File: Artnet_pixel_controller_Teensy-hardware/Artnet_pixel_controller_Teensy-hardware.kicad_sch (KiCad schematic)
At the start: 37 parts, among them J1 Barrel_Jack_Switch, J10 Conn_01x02_Pin, J2 HR871181A, J3 Conn_01x02_Pin, J4 Conn_01x02_Pin, J5 Conn_01x02_Pin, J6 Conn_01x02_Pin, J7 Conn_01x02_Pin, J8 Conn_01x02_Pin, J9 Conn_01x02_Pin, Q1 AO3401A, SW1 SW_DIP_x08, U1 R-785.0-1.0, U3 74HC245

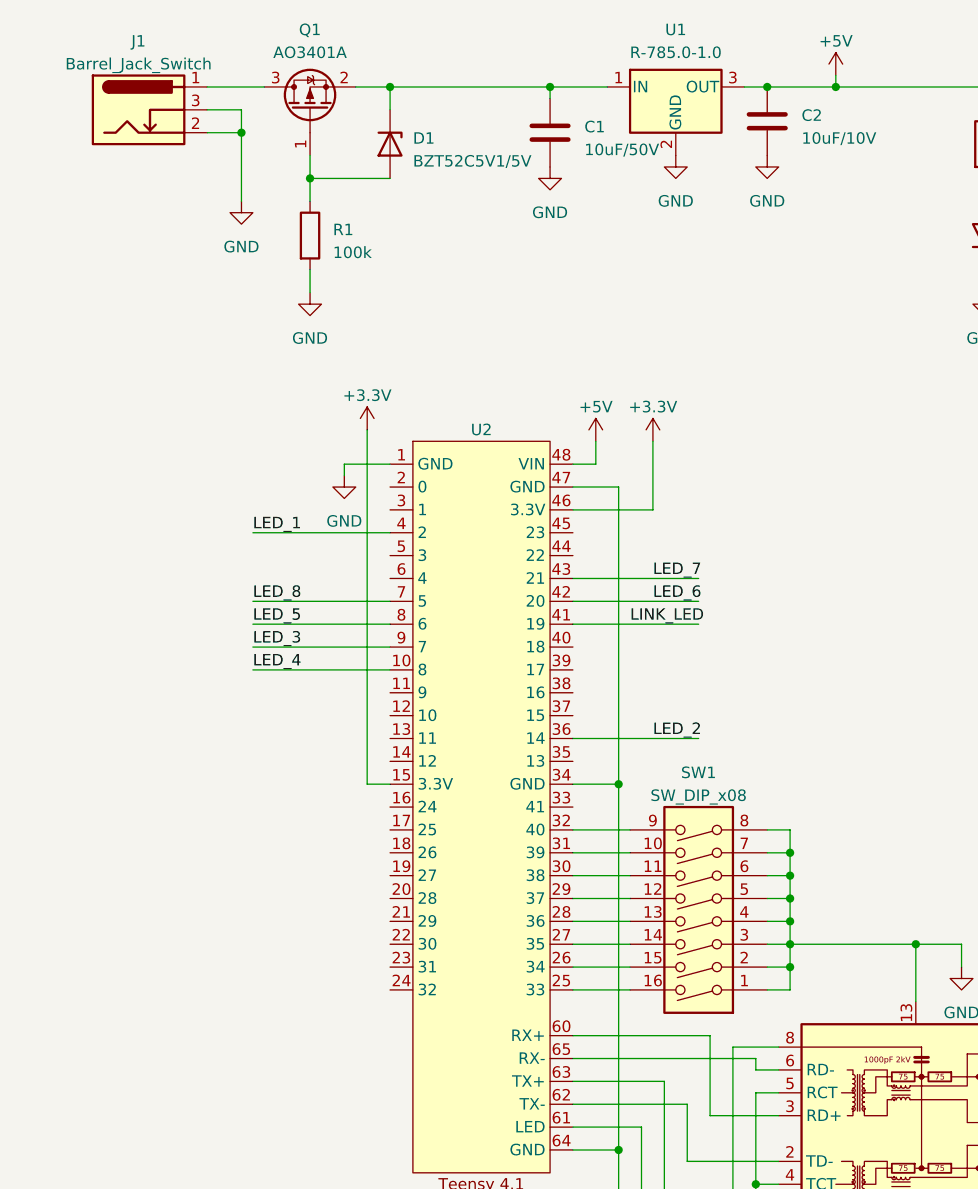
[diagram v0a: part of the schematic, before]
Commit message: WS2812Serial用のピン配置に変更
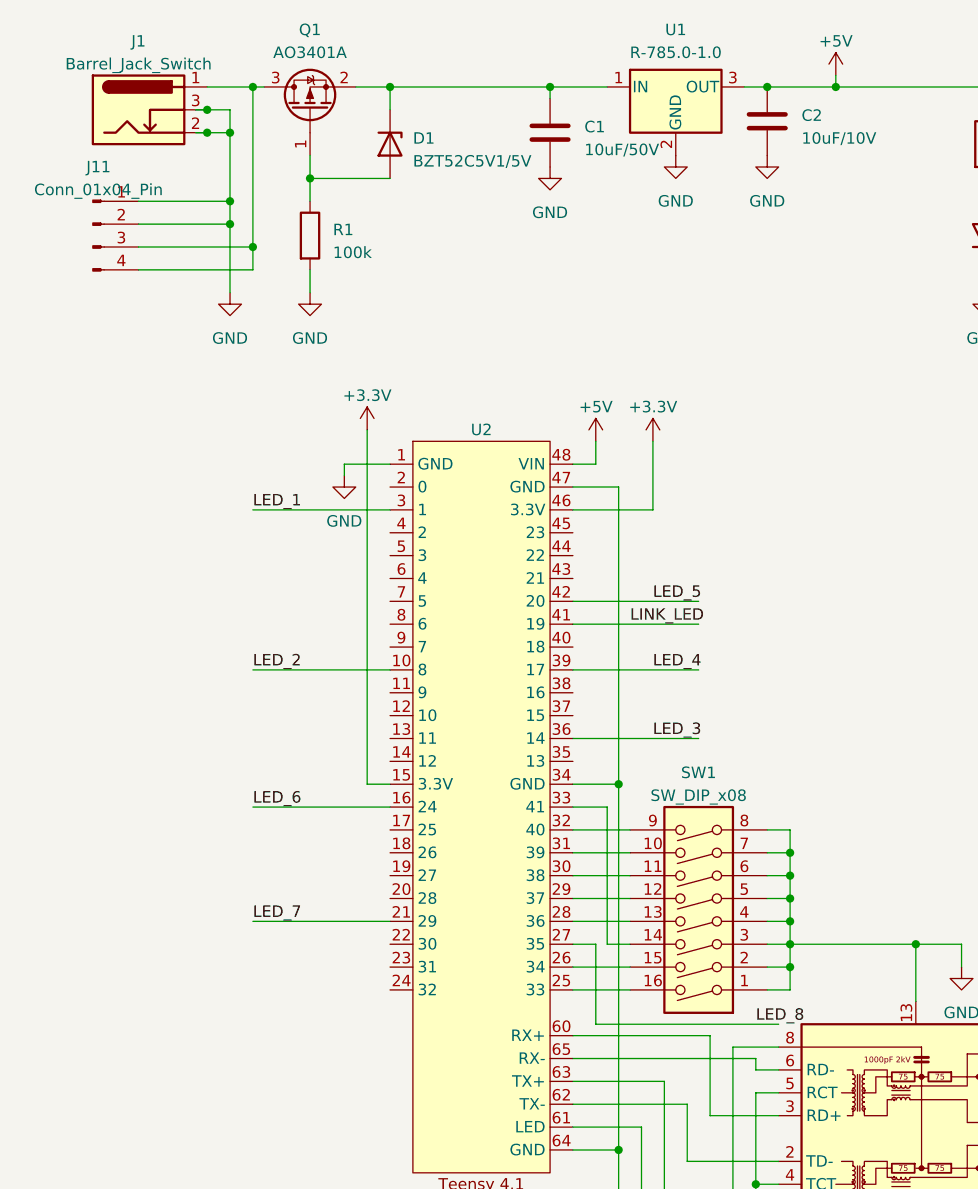
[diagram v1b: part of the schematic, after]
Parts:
- added J11: Conn_01x04_Pin, Connector_Phoenix_MC:PhoenixContact_MC_1,5_4-G-3.81_1x04_P3.81mm_Horizontal, symbol Connector:Conn_01x04_Pin
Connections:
- net GND: now also J11.1 (Pin_1), J11.2 (Pin_2)
- net LED_1: now also U2.3 (1); no longer U2.4 (2)
- net LED_2: now also U2.10 (8); no longer U2.36 (14)
- net LED_3: now also U2.36 (14); no longer U2.9 (7)
- net LED_4: now also U2.39 (17); no longer U2.10 (8)
- net LED_5: now also U2.42 (20); no longer U2.8 (6)
- net LED_6: now also U2.16 (24); no longer U2.42 (20)
- net LED_7: now also U2.21 (29); no longer U2.43 (21)
- net LED_8: now also U2.27 (35); no longer U2.7 (5)
- net at J1.1, Q1.3 (D): now also J11.3 (Pin_3), J11.4 (Pin_4)
- net at SW1.14: now also U2.33 (41); no longer U2.27 (35)
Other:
- company: (none) -> Ponoor Experiments inc.
- title: (none) -> Artnet pixel led controller with Teensy4.1

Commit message: プロト基板入稿データ
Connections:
- net +3.3V: no longer names the net of U2.15 (3.3V)
- net +3.3V: no longer U2.46 (3.3V)
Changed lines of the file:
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@@
-    (stroke (width 0) (type default))
-  )
-  (wire (pts (xy 60.96 106.68) (xy 58.42 106.68))
     (stroke (width 0) (type default))
   )
@@
     (stroke (width 0) (type default))
   )
-  (wire (pts (xy 81.28 76.2) (xy 90.17 76.2))
-    (stroke (width 0) (type default))
-  )
   (wire (pts (xy 52.07 49.53) (xy 52.07 52.07))
     (stroke (width 0) (type default))
@@
     (stroke (width 0) (type default))
   )
-  (wire (pts (xy 90.17 68.58) (xy 90.17 76.2))
-    (stroke (width 0) (type default))
-  )
   (wire (pts (xy 227.33 71.12) (xy 233.68 71.12))
     (stroke (width 0) (type default))
@@
   )
   (wire (pts (xy 81.28 106.68) (xy 86.36 106.68))
-    (stroke (width 0) (type default))
-  )
-  (wire (pts (xy 58.42 106.68) (xy 58.42 67.31))
     (stroke (width 0) (type default))
   )
@@
         (path "/92745dad-aaf3-4218-9787-63c390caac23"
           (reference "H5") (unit 1)
-        )
-      )
-    )
-  )
-  (symbol (lib_id "power:+3.3V") (at 90.17 68.58 0) (unit 1)
-    (in_bom yes) (on_board yes) (dnp no) (fields_autoplaced)
-    (property "Reference" "#PWR09" (at 90.17 72.39 0)
-      (effects (font (size 1.27 1.27)) hide)
-    )
-    (property "Value" "+3.3V" (at 90.17 64.77 0)
-      (effects (font (size 1.27 1.27)))
-    )
-    (property "Footprint" "" (at 90.17 68.58 0)
-      (effects (font (size 1.27 1.27)) hide)
-    )
-    (property "Datasheet" "" (at 90.17 68.58 0)
-      (effects (font (size 1.27 1.27)) hide)
-    )
-    (pin "1")
-    (instances
-      (project "Artnet_pixel_controller_Teensy-hardware"
-        (path "/92745dad-aaf3-4218-9787-63c390caac23"
-          (reference "#PWR09") (unit 1)
         )
       )
@@
         )
       )
-    )
-  )
-  (symbol (lib_id "power:+3.3V") (at 58.42 67.31 0) (unit 1)
-    (in_bom yes) (on_board yes) (dnp no) (fields_autoplaced)
-    (property "Reference" "#PWR011" (at 58.42 71.12 0)
-      (effects (font (size 1.27 1.27)) hide)
-    )
-    (property "Value" "+3.3V" (at 58.42 63.5 0)
-      (effects (font (size 1.27 1.27)))
-    )
-    (property "Footprint" "" (at 58.42 67.31 0)
-      (effects (font (size 1.27 1.27)) hide)
-    )
-    (property "Datasheet" "" (at 58.42 67.31 0)
-      (effects (font (size 1.27 1.27)) hide)
-    )
-    (pin "1")
-    (instances
-      (project "Artnet_pixel_controller_Teensy-hardware"
-        (path "/92745dad-aaf3-4218-9787-63c390caac23"
-          (reference "#PWR011") (unit 1)
-        )
-      )

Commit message: gerber data v1.0.0
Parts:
- R1: value 100k -> 10k
- R11: value 1k -> 10k
- R2: value 150 -> 220
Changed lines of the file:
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@@
       (effects (font (size 1.27 1.27)) (justify left))
     )
-    (property "Value" "1k" (at 129.54 37.465 0)
+    (property "Value" "10k" (at 129.54 37.465 0)
       (effects (font (size 1.27 1.27)) (justify left))
     )
@@
       (effects (font (size 1.27 1.27)))
     )
-    (property "Value" "150" (at 129.54 165.1 90)
+    (property "Value" "220" (at 129.54 165.1 90)
       (effects (font (size 1.27 1.27)))
     )
@@
       (effects (font (size 1.27 1.27)) (justify left))
     )
-    (property "Value" "100k" (at 54.61 47.625 0)
-      (effects (font (size 1.27 1.27)) (justify left))
-    )
+    (property "Value" "10k" (at 54.61 47.625 0)
+      (effects (font (size 1.27 1.27)) (justify left))
+    )

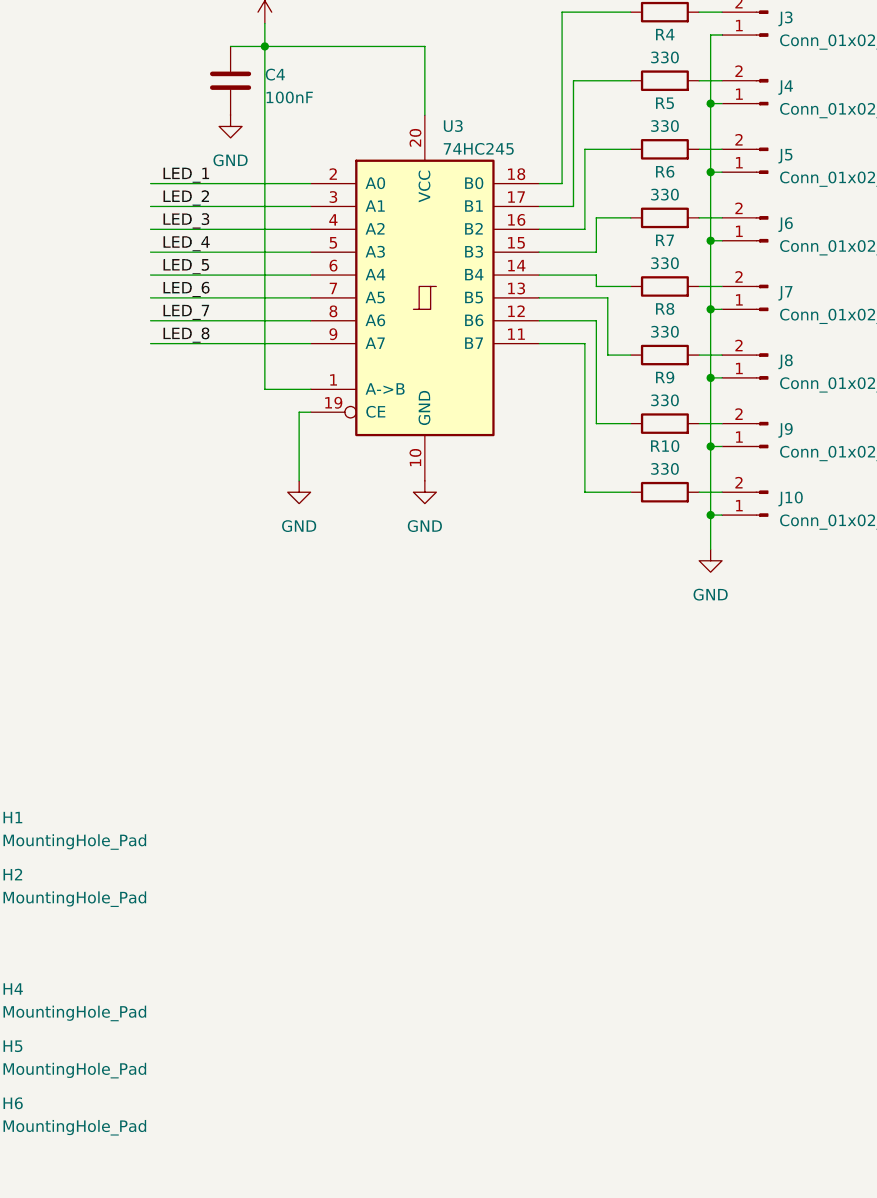
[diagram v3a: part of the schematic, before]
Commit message: LED出力の番号を入れ替え
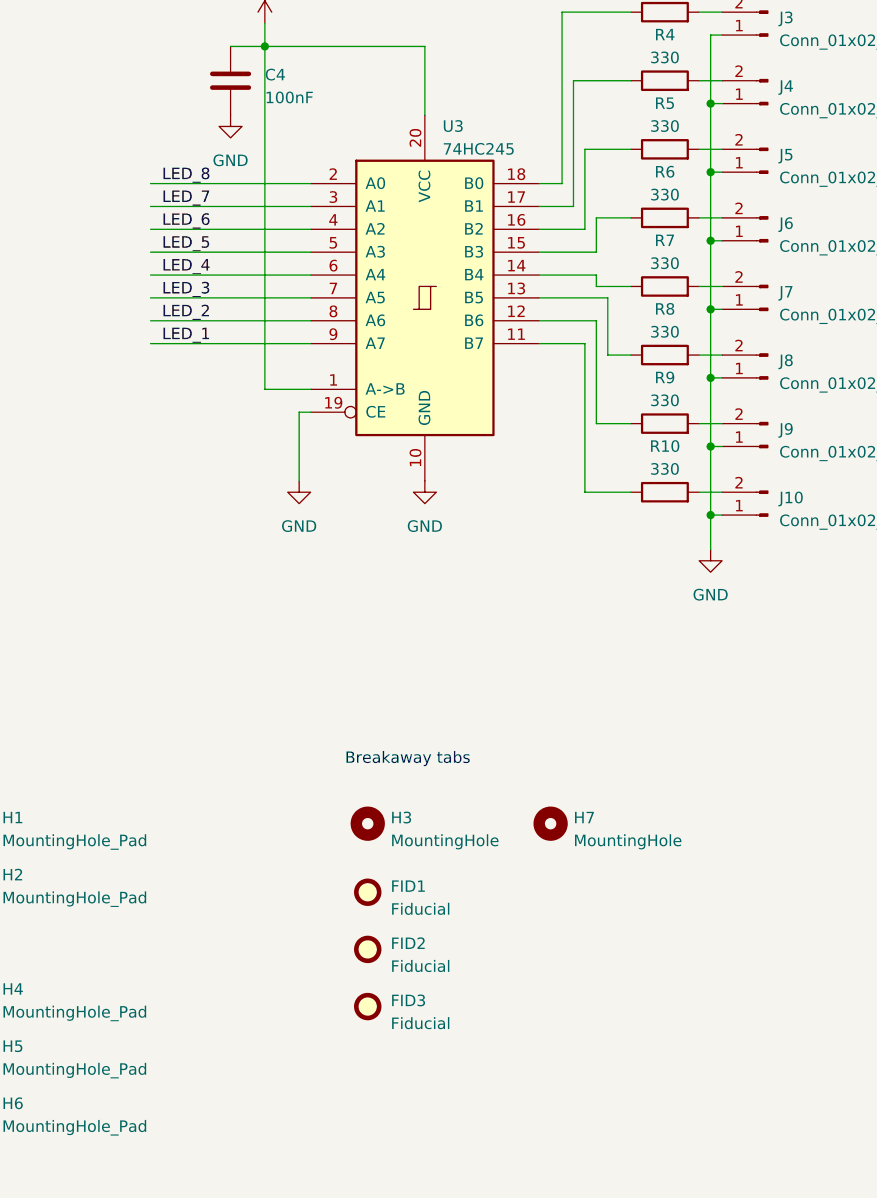
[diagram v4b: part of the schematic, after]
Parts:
- added FID1, FID2, FID3: Fiducial, Fiducial:Fiducial_1mm_Mask3mm, symbol Mechanical:Fiducial
- added H3, H7: MountingHole, MountingHole:MountingHole_4mm, symbol Mechanical:MountingHole
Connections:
- net LED_1: now also U3.9 (A7); no longer U3.2 (A0)
- net LED_2: now also U3.8 (A6); no longer U3.3 (A1)
- net LED_3: now also U3.7 (A5); no longer U3.4 (A2)
- net LED_4: now also U3.6 (A4); no longer U3.5 (A3)
- net LED_5: now also U3.5 (A3); no longer U3.6 (A4)
- net LED_6: now also U3.4 (A2); no longer U3.7 (A5)
- net LED_7: now also U3.3 (A1); no longer U3.8 (A6)
- net LED_8: now also U3.2 (A0); no longer U3.9 (A7)
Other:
- note added: "Breakaway tabs"
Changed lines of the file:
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@@
     (stroke (width 0) (type default))
   )
+  (text "Breakaway tabs" (at 205.74 120.65 0)
+    (effects (font (size 1.27 1.27)) (justify left bottom))
+  )
   (label "LED_1" (at 45.72 76.2 0) (fields_autoplaced)
     (effects (font (size 1.27 1.27)) (justify left bottom))
@@
     (effects (font (size 1.27 1.27)) (justify left bottom))
   )
-  (label "LED_2" (at 185.42 58.42 0) (fields_autoplaced)
+  (label "LED_7" (at 185.42 58.42 0) (fields_autoplaced)
     (effects (font (size 1.27 1.27)) (justify left bottom))
   )
@@
     (effects (font (size 1.27 1.27)) (justify left bottom))
   )
-  (label "LED_5" (at 185.42 66.04 0) (fields_autoplaced)
+  (label "LED_4" (at 185.42 66.04 0) (fields_autoplaced)
     (effects (font (size 1.27 1.27)) (justify left bottom))
   )
@@
     (effects (font (size 1.27 1.27)) (justify left bottom))
   )
-  (label "LED_4" (at 185.42 63.5 0) (fields_autoplaced)
+  (label "LED_5" (at 185.42 63.5 0) (fields_autoplaced)
     (effects (font (size 1.27 1.27)) (justify left bottom))
   )
@@
     (effects (font (size 1.27 1.27)) (justify left bottom))
   )
-  (label "LED_1" (at 185.42 55.88 0) (fields_autoplaced)
-    (effects (font (size 1.27 1.27)) (justify left bottom))
-  )
-  (label "LED_3" (at 185.42 60.96 0) (fields_autoplaced)
+  (label "LED_8" (at 185.42 55.88 0) (fields_autoplaced)
+    (effects (font (size 1.27 1.27)) (justify left bottom))
+  )
+  (label "LED_6" (at 185.42 60.96 0) (fields_autoplaced)
     (effects (font (size 1.27 1.27)) (justify left bottom))
   )
@@
     (effects (font (size 1.27 1.27)) (justify left bottom))
   )
-  (label "LED_7" (at 185.42 71.12 0) (fields_autoplaced)
+  (label "LED_2" (at 185.42 71.12 0) (fields_autoplaced)
     (effects (font (size 1.27 1.27)) (justify left bottom))
   )
@@
     (effects (font (size 1.27 1.27)) (justify left bottom))
   )
-  (label "LED_6" (at 185.42 68.58 0) (fields_autoplaced)
-    (effects (font (size 1.27 1.27)) (justify left bottom))
-  )
-  (label "LED_8" (at 185.42 73.66 0) (fields_autoplaced)
+  (label "LED_3" (at 185.42 68.58 0) (fields_autoplaced)
+    (effects (font (size 1.27 1.27)) (justify left bottom))
+  )
+  (label "LED_1" (at 185.42 73.66 0) (fields_autoplaced)
     (effects (font (size 1.27 1.27)) (justify left bottom))
   )
@@
     )
   )
+  (symbol (lib_id "Mechanical:MountingHole") (at 228.6 127 0) (unit 1)
+    (in_bom yes) (on_board yes) (dnp no) (fields_autoplaced)
+    (property "Reference" "H7" (at 231.14 126.365 0)
+      (effects (font (size 1.27 1.27)) (justify left))
+    )
+    (property "Value" "MountingHole" (at 231.14 128.905 0)
+      (effects (font (size 1.27 1.27)) (justify left))
+    )
+    (property "Footprint" "MountingHole:MountingHole_4mm" (at 228.6 127 0)
+      (effects (font (size 1.27 1.27)) hide)
+    )
+    (property "Datasheet" "~" (at 228.6 127 0)
+      (effects (font (size 1.27 1.27)) hide)
+    )
+    (instances
+      (project "Artnet_pixel_controller_Teensy-hardware"
+        (path "/92745dad-aaf3-4218-9787-63c390caac23"
+          (reference "H7") (unit 1)
+        )
+      )
+    )
+  )
   (symbol (lib_id "Mechanical:MountingHole_Pad") (at 163.83 127 270) (unit 1)
     (in_bom yes) (on_board yes) (dnp no) (fields_autoplaced)
@@
         (path "/92745dad-aaf3-4218-9787-63c390caac23"
           (reference "#PWR01") (unit 1)
+        )
+      )
+    )
+  )
+  (symbol (lib_id "Mechanical:Fiducial") (at 208.28 134.62 0) (unit 1)
+    (in_bom yes) (on_board yes) (dnp no) (fields_autoplaced)
+    (property "Reference" "FID1" (at 210.82 133.985 0)
+      (effects (font (size 1.27 1.27)) (justify left))
+    )
+    (property "Value" "Fiducial" (at 210.82 136.525 0)
+      (effects (font (size 1.27 1.27)) (justify left))
+    )
+    (property "Footprint" "Fiducial:Fiducial_1mm_Mask3mm" (at 208.28 134.62 0)
+      (effects (font (size 1.27 1.27)) hide)
+    )
+    (property "Datasheet" "~" (at 208.28 134.62 0)
+      (effects (font (size 1.27 1.27)) hide)
+    )
+    (instances
+      (project "Artnet_pixel_controller_Teensy-hardware"
+        (path "/92745dad-aaf3-4218-9787-63c390caac23"
+          (reference "FID1") (unit 1)
         )
       )
@@
     )
   )
+  (symbol (lib_id "Mechanical:Fiducial") (at 208.28 140.97 0) (unit 1)
+    (in_bom yes) (on_board yes) (dnp no) (fields_autoplaced)
+    (property "Reference" "FID2" (at 210.82 140.335 0)
+      (effects (font (size 1.27 1.27)) (justify left))
+    )
+    (property "Value" "Fiducial" (at 210.82 142.875 0)
+      (effects (font (size 1.27 1.27)) (justify left))
+    )
+    (property "Footprint" "Fiducial:Fiducial_1mm_Mask3mm" (at 208.28 140.97 0)
+      (effects (font (size 1.27 1.27)) hide)
+    )
+    (property "Datasheet" "~" (at 208.28 140.97 0)
+      (effects (font (size 1.27 1.27)) hide)
+    )
+    (instances
+      (project "Artnet_pixel_controller_Teensy-hardware"
+        (path "/92745dad-aaf3-4218-9787-63c390caac23"
+          (reference "FID2") (unit 1)
+        )
+      )
+    )
+  )
   (symbol (lib_id "Device:R") (at 127 35.56 0) (unit 1)
     (in_bom yes) (on_board yes) (dnp no) (fields_autoplaced)
@@
         (path "/92745dad-aaf3-4218-9787-63c390caac23"
           (reference "R11") (unit 1)
+        )
+      )
+    )
+  )
+  (symbol (lib_id "Mechanical:Fiducial") (at 208.28 147.32 0) (unit 1)
+    (in_bom yes) (on_board yes) (dnp no) (fields_autoplaced)
+    (property "Reference" "FID3" (at 210.82 146.685 0)
+      (effects (font (size 1.27 1.27)) (justify left))
+    )
+    (property "Value" "Fiducial" (at 210.82 149.225 0)
+      (effects (font (size 1.27 1.27)) (justify left))
+    )
+    (property "Footprint" "Fiducial:Fiducial_1mm_Mask3mm" (at 208.28 147.32 0)
+      (effects (font (size 1.27 1.27)) hide)
+    )
+    (property "Datasheet" "~" (at 208.28 147.32 0)
+      (effects (font (size 1.27 1.27)) hide)
+    )
+    (instances
+      (project "Artnet_pixel_controller_Teensy-hardware"
+        (path "/92745dad-aaf3-4218-9787-63c390caac23"
+          (reference "FID3") (unit 1)
         )
       )
@@
         )
       )
+    )
+  )
+  (symbol (lib_id "Mechanical:MountingHole") (at 208.28 127 0) (unit 1)
+    (in_bom yes) (on_board yes) (dnp no) (fields_autoplaced)
+    (property "Reference" "H3" (at 210.82 126.365 0)
+      (effects (font (size 1.27 1.27)) (justify left))
+    )
+    (property "Value" "MountingHole" (at 210.82 128.905 0)
+      (effects (font (size 1.27 1.27)) (justify left))
+    )
+    (property "Footprint" "MountingHole:MountingHole_4mm" (at 208.28 127 0)
+      (effects (font (size 1.27 1.27)) hide)
+    )
+    (property "Datasheet" "~" (at 208.28 127 0)
+      (effects (font (size 1.27 1.27)) hide)
+    )
+    (instances
+      (project "Artnet_pixel_controller_Teensy-hardware"
+        (path "/92745dad-aaf3-4218-9787-63c390caac23"
+          (reference "H3") (unit 1)
+        )
+      )
